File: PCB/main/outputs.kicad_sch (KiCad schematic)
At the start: 0 parts

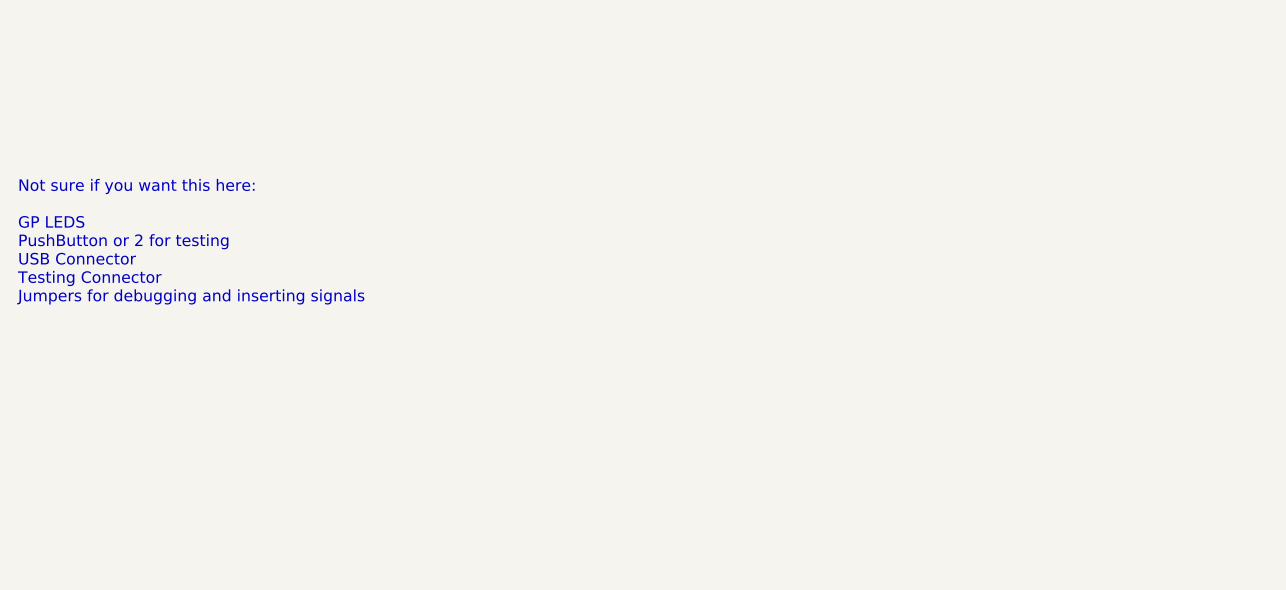
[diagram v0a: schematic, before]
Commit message: changed power schematic
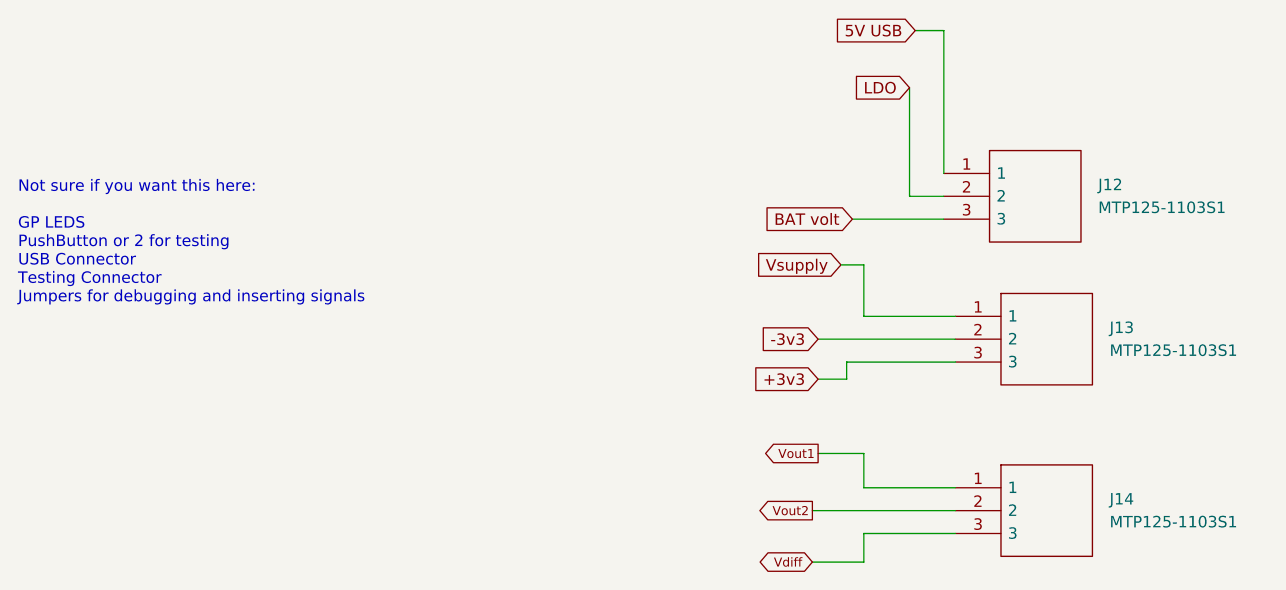
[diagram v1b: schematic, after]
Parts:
- added J12, J13, J14: MTP125-1103S1, SamacSys_Parts:HDRV3W64P0X254_1X3_762X250X885P, symbol SamacSys_Parts_power:MTP125-1103S1
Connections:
- new net +3v3: J13.3
- new net -3v3: J13.2
- new net 5V USB: J12.1
- new net BAT volt: J12.3
- new net LDO: J12.2
- new net Vdiff: J14.3
- new net Vout1: J14.1
- new net Vout2: J14.2
- new net Vsupply: J13.1

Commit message: NEW PCB ADDED
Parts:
- J12, J13, J14: Comment (none) -> pin header (3x1); LCSC (none) -> C358685
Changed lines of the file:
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@@
       (effects (font (size 1.27 1.27)) (justify left) hide)
+    )
+    (property "Comment" "pin header (3x1)" (id 12) (at 229.235 71.755 0)
+      (effects (font (size 1.27 1.27)) hide)
+    )
+    (property "LCSC" "C358685" (id 13) (at 229.235 71.755 0)
+      (effects (font (size 1.27 1.27)) hide)
     )
     (pin "1")
@@
       (effects (font (size 1.27 1.27)) (justify left) hide)
     )
+    (property "Comment" "pin header (3x1)" (id 12) (at 230.505 87.63 0)
+      (effects (font (size 1.27 1.27)) hide)
+    )
+    (property "LCSC" "C358685" (id 13) (at 230.505 87.63 0)
+      (effects (font (size 1.27 1.27)) hide)
+    )
     (pin "1")
     (pin "2")
@@
       (effects (font (size 1.27 1.27)) (justify left) hide)
     )
+    (property "Comment" "pin header (3x1)" (id 12) (at 230.505 106.68 0)
+      (effects (font (size 1.27 1.27)) hide)
+    )
+    (property "LCSC" "C358685" (id 13) (at 230.505 106.68 0)
+      (effects (font (size 1.27 1.27)) hide)
+    )
     (pin "1")
